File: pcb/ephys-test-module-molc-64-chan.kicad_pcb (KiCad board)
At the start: 2 copper layers, 100 x 60 mm, 12 parts, among them J1 MOLC-110-01-S-Q_1, J2 MOLC-110-01-S-Q_1, J3 Conn_02x02_Odd_Even, J4 BSE-040-01-F-D-A-TR, J5 BSE-040-01-F-D-A-TR, U1 AT24C64D-SSHM-T

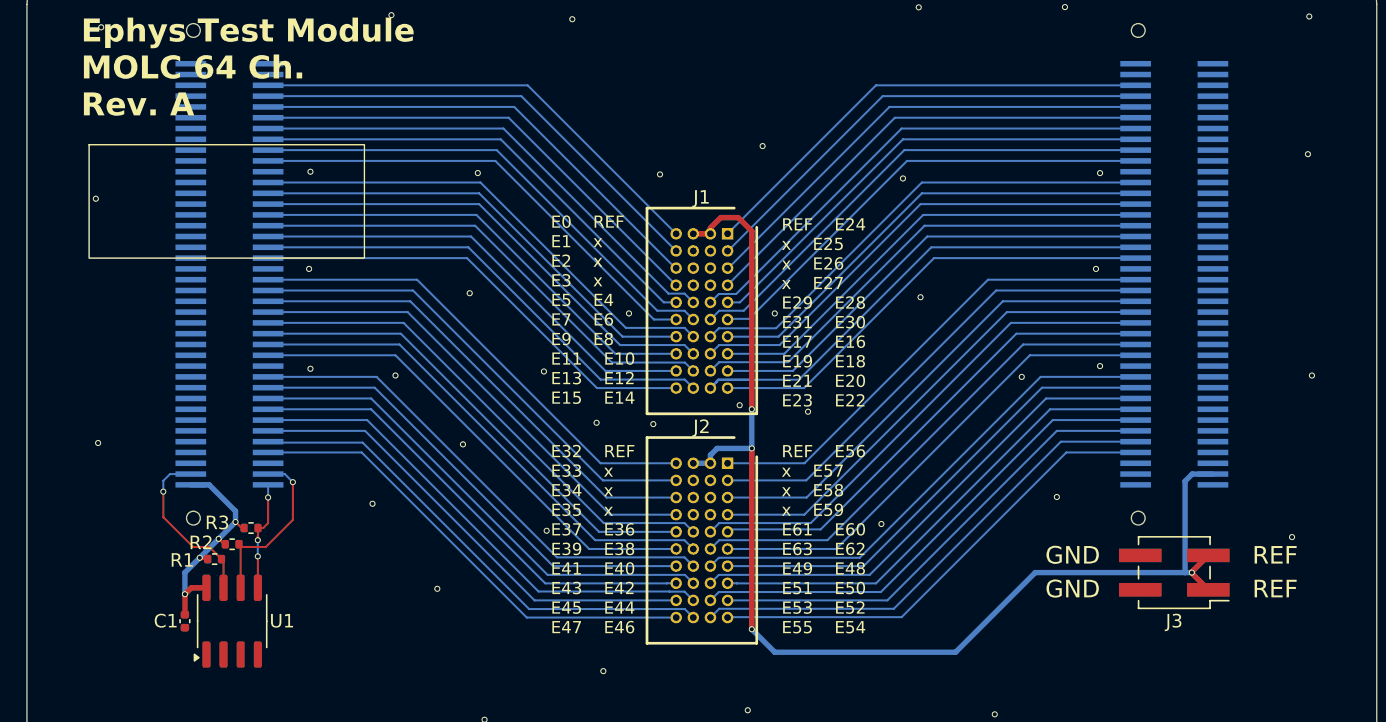
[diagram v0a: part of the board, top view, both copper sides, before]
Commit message: Revision B
- Added 220k resistor arrays in series with amplifier connections to
  simulate electrodes
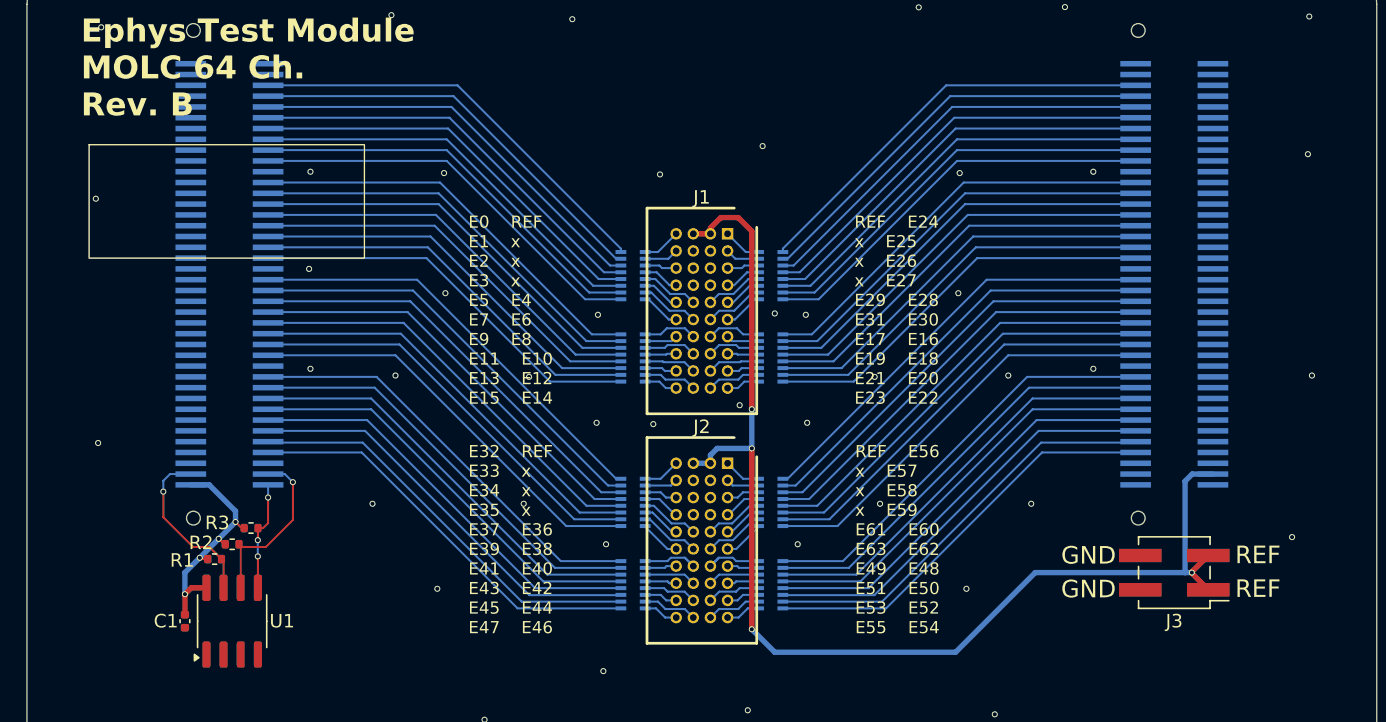
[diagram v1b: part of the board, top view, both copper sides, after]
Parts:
- added RN1: 220k, Resistor_SMD:R_Array_Convex_8x0602, B.Cu at (152.9, 123.0)
- added RN2: 220k, Resistor_SMD:R_Array_Convex_8x0602, B.Cu at (152.9, 116.9)
- added RN3: 220k, Resistor_SMD:R_Array_Convex_8x0602, B.Cu at (152.9, 106.2)
- added RN4: 220k, Resistor_SMD:R_Array_Convex_8x0602, B.Cu at (152.9, 100.1)
- added RN5: 220k, Resistor_SMD:R_Array_Convex_8x0602, B.Cu at (163.1, 116.9)
- added RN6: 220k, Resistor_SMD:R_Array_Convex_8x0602, B.Cu at (163.1, 100.1)
- added RN7: 220k, Resistor_SMD:R_Array_Convex_8x0602, B.Cu at (163.1, 123.0)
- added RN8: 220k, Resistor_SMD:R_Array_Convex_8x0602, B.Cu at (163.1, 106.2)
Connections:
- J1 pad A1: /Headstage Interface/B8.E_{0} -> /Headstage Interface/E24
- J1 pad A10: /Headstage Interface/B9.E_{7} -> /Headstage Interface/E22
- J1 pad A2: /Headstage Interface/B8.E_{1} -> /Headstage Interface/E25
- J1 pad A3: /Headstage Interface/B8.E_{2} -> /Headstage Interface/E26
- J1 pad A4: /Headstage Interface/B8.E_{3} -> /Headstage Interface/E27
- J1 pad A5: /Headstage Interface/B8.E_{5} -> /Headstage Interface/E28
- J1 pad A6: /Headstage Interface/B8.E_{7} -> /Headstage Interface/E30
- J1 pad A7: /Headstage Interface/B9.E_{1} -> /Headstage Interface/E16
- J1 pad A8: /Headstage Interface/B9.E_{3} -> /Headstage Interface/E18
- J1 pad A9: /Headstage Interface/B9.E_{5} -> /Headstage Interface/E20
- J1 pad B10: /Headstage Interface/B9.E_{6} -> /Headstage Interface/E23
- J1 pad B5: /Headstage Interface/B8.E_{4} -> /Headstage Interface/E29
- J1 pad B6: /Headstage Interface/B8.E_{6} -> /Headstage Interface/E31
- J1 pad B7: /Headstage Interface/B9.E_{0} -> /Headstage Interface/E17
- J1 pad B8: /Headstage Interface/B9.E_{2} -> /Headstage Interface/E19
- J1 pad B9: /Headstage Interface/B9.E_{4} -> /Headstage Interface/E21
- J1 pad C10: /Headstage Interface/B5.E_{6} -> /Headstage Interface/E14
- J1 pad C5: /Headstage Interface/B4.E_{4} -> /Headstage Interface/E4
- J1 pad C6: /Headstage Interface/B4.E_{6} -> /Headstage Interface/E6
- J1 pad C7: /Headstage Interface/B5.E_{0} -> /Headstage Interface/E8
- J1 pad C8: /Headstage Interface/B5.E_{2} -> /Headstage Interface/E10
- J1 pad C9: /Headstage Interface/B5.E_{4} -> /Headstage Interface/E12
- J1 pad D1: /Headstage Interface/B4.E_{0} -> /Headstage Interface/E0
- J1 pad D10: /Headstage Interface/B5.E_{7} -> /Headstage Interface/E15
- J1 pad D2: /Headstage Interface/B4.E_{1} -> /Headstage Interface/E1
- J1 pad D3: /Headstage Interface/B4.E_{2} -> /Headstage Interface/E2
- J1 pad D4: /Headstage Interface/B4.E_{3} -> /Headstage Interface/E3
- J1 pad D5: /Headstage Interface/B4.E_{5} -> /Headstage Interface/E5
- J1 pad D6: /Headstage Interface/B4.E_{7} -> /Headstage Interface/E7
- J1 pad D7: /Headstage Interface/B5.E_{1} -> /Headstage Interface/E9
- J1 pad D8: /Headstage Interface/B5.E_{3} -> /Headstage Interface/E11
- J1 pad D9: /Headstage Interface/B5.E_{5} -> /Headstage Interface/E13
- J2 pad A1: /Headstage Interface/B10.E_{0} -> /Headstage Interface/E56
- J2 pad A10: /Headstage Interface/B11.E_{7} -> /Headstage Interface/E54
- J2 pad A2: /Headstage Interface/B10.E_{1} -> /Headstage Interface/E57
- J2 pad A3: /Headstage Interface/B10.E_{2} -> /Headstage Interface/E58
- J2 pad A4: /Headstage Interface/B10.E_{3} -> /Headstage Interface/E59
- J2 pad A5: /Headstage Interface/B10.E_{5} -> /Headstage Interface/E60
- J2 pad A6: /Headstage Interface/B10.E_{7} -> /Headstage Interface/E62
- J2 pad A7: /Headstage Interface/B11.E_{1} -> /Headstage Interface/E48
- J2 pad A8: /Headstage Interface/B11.E_{3} -> /Headstage Interface/E50
- J2 pad A9: /Headstage Interface/B11.E_{5} -> /Headstage Interface/E52
- J2 pad B10: /Headstage Interface/B11.E_{6} -> /Headstage Interface/E55
- J2 pad B5: /Headstage Interface/B10.E_{4} -> /Headstage Interface/E61
- J2 pad B6: /Headstage Interface/B10.E_{6} -> /Headstage Interface/E63
- J2 pad B7: /Headstage Interface/B11.E_{0} -> /Headstage Interface/E49
- J2 pad B8: /Headstage Interface/B11.E_{2} -> /Headstage Interface/E51
- J2 pad B9: /Headstage Interface/B11.E_{4} -> /Headstage Interface/E53
- J2 pad C10: /Headstage Interface/B7.E_{6} -> /Headstage Interface/E46
- J2 pad C5: /Headstage Interface/B6.E_{4} -> /Headstage Interface/E36
- J2 pad C6: /Headstage Interface/B6.E_{6} -> /Headstage Interface/E38
- J2 pad C7: /Headstage Interface/B7.E_{0} -> /Headstage Interface/E40
- J2 pad C8: /Headstage Interface/B7.E_{2} -> /Headstage Interface/E42
- J2 pad C9: /Headstage Interface/B7.E_{4} -> /Headstage Interface/E44
- J2 pad D1: /Headstage Interface/B6.E_{0} -> /Headstage Interface/E32
- J2 pad D10: /Headstage Interface/B7.E_{7} -> /Headstage Interface/E47
- J2 pad D2: /Headstage Interface/B6.E_{1} -> /Headstage Interface/E33
- J2 pad D3: /Headstage Interface/B6.E_{2} -> /Headstage Interface/E34
- J2 pad D4: /Headstage Interface/B6.E_{3} -> /Headstage Interface/E35
- J2 pad D5: /Headstage Interface/B6.E_{5} -> /Headstage Interface/E37
- J2 pad D6: /Headstage Interface/B6.E_{7} -> /Headstage Interface/E39
- J2 pad D7: /Headstage Interface/B7.E_{1} -> /Headstage Interface/E41
- J2 pad D8: /Headstage Interface/B7.E_{3} -> /Headstage Interface/E43
- J2 pad D9: /Headstage Interface/B7.E_{5} -> /Headstage Interface/E45
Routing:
- net /Headstage Interface/B9.E_{6}: track 39.0 -> 30.1 mm
- net /Headstage Interface/B6.E_{6}: track 37.8 -> 31.5 mm
- net /Headstage Interface/B10.E_{6}: track 37.8 -> 31.5 mm
- net /Headstage Interface/B4.E_{6}: track 36.7 -> 30.5 mm
- net /Headstage Interface/B8.E_{6}: track 36.7 -> 30.5 mm
- net /Headstage Interface/B6.E_{4}: track 37.9 -> 31.7 mm
- net /Headstage Interface/B10.E_{4}: track 37.9 -> 31.7 mm
- net /Headstage Interface/B4.E_{4}: track 36.8 -> 30.8 mm
- net /Headstage Interface/B8.E_{4}: track 36.8 -> 30.8 mm
- net /Headstage Interface/B11.E_{6}: track 36.9 -> 30.9 mm
- net /Headstage Interface/B7.E_{6}: track 36.8 -> 30.9 mm
- net /Headstage Interface/B5.E_{6}: track 35.8 -> 30.1 mm
- net /Headstage Interface/B7.E_{4}: track 37.0 -> 31.3 mm
- net /Headstage Interface/B11.E_{4}: track 37.0 -> 31.3 mm
- net /Headstage Interface/B9.E_{4}: track 36.0 -> 30.3 mm
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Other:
- board text added: "Ephys Test Module MOLC 64 Ch. Rev. B"
- board text removed: "Ephys Test Module MOLC 64 Ch. Rev. A"

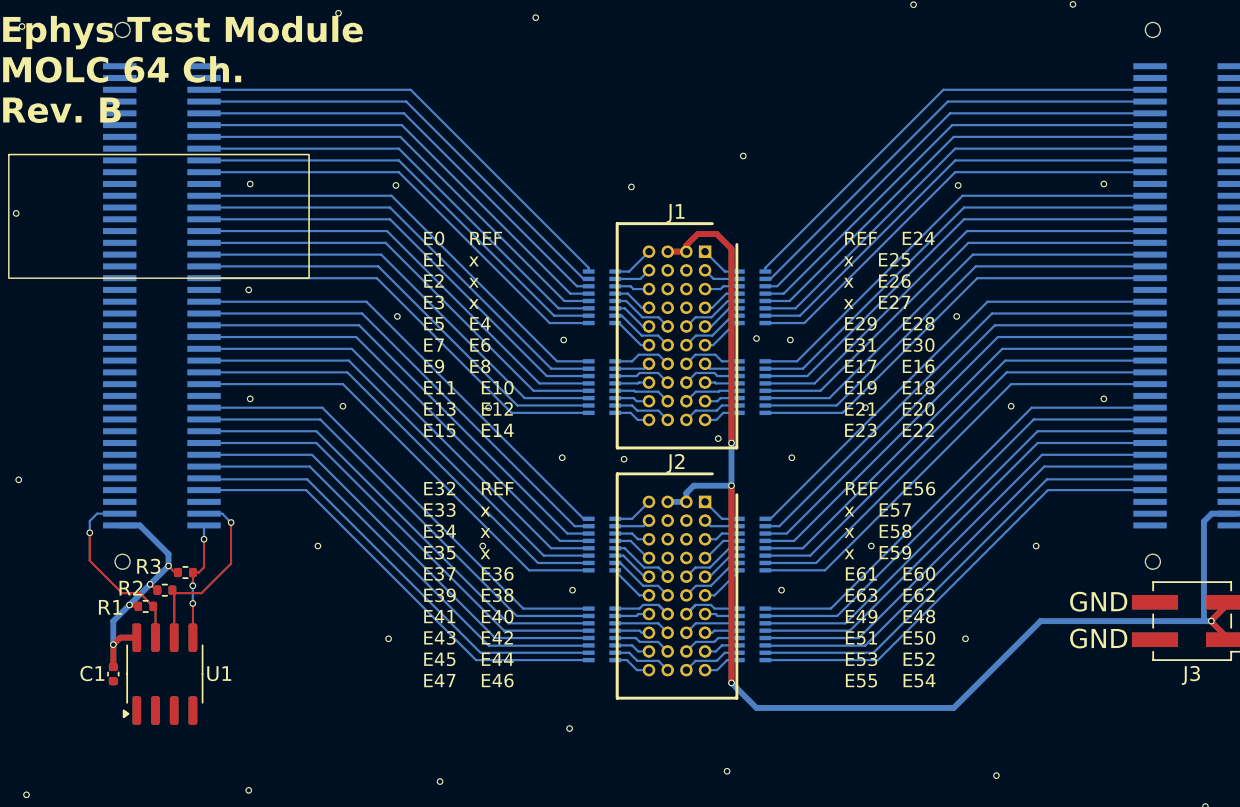
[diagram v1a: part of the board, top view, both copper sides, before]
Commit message: Revision B
- Widened traces to 0.2 mm
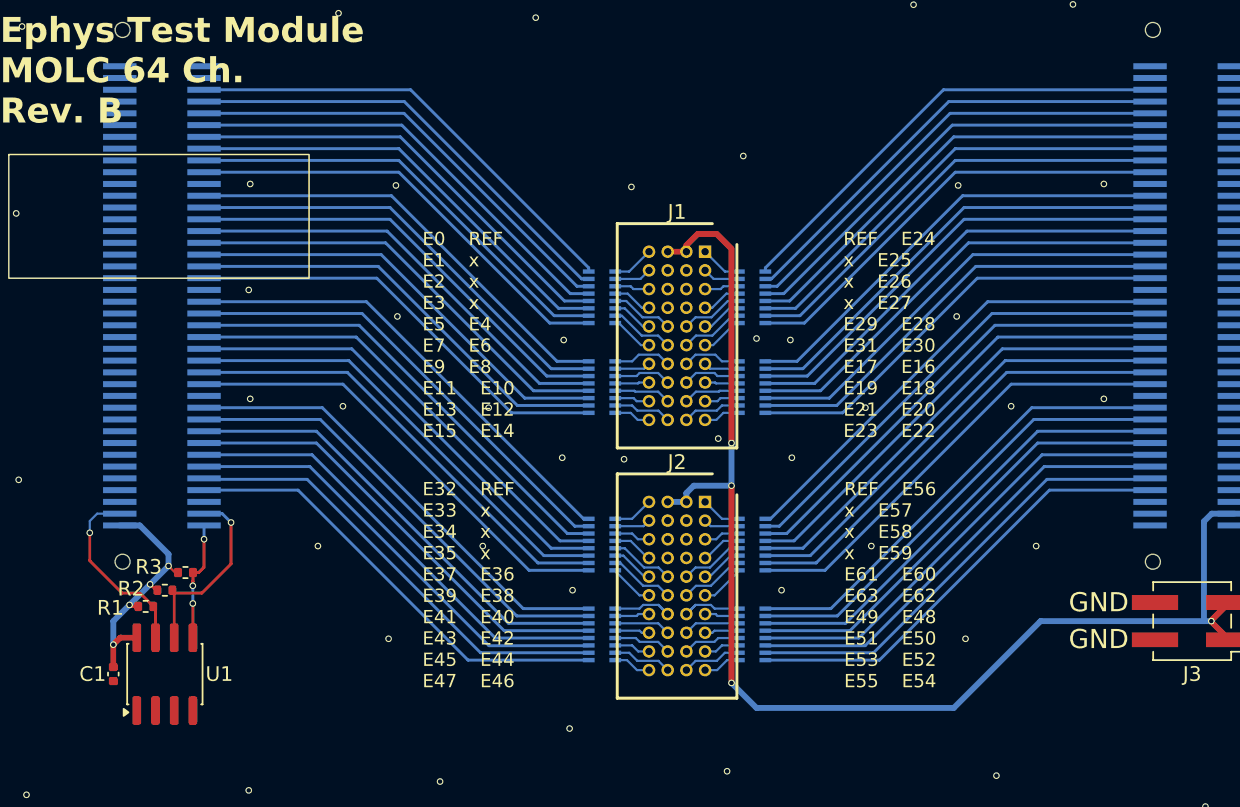
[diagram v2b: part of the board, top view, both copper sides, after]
